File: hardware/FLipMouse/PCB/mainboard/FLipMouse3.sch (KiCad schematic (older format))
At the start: 85 parts, among them J1 SJ2-3574A, J2 SJ2-3574A, J3 M50-3900542, J4 Conn_ARM_JTAG_SWD_10, J5 Conn_02x05_Odd_Even, J6 USB_OTG, J7 Conn_01x06, Q1 BC847, Q2 BC847, Q3 BSH108, Q4 BSH108, Q5 BSH108, SW1 SW_Push, SW2 SW_Push, U1 ESP32-WROOM, U2 TSOP4838, U3 LPC11U24FBD, U4 TSR_1-2433, U5 MPXV7007GP, Y1 JA-12.000-18-DFE

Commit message: changed schematic for prototyp B: -) Added VPP as 3v3, always on (supplied by a new LDO) -) Removed GNDD, one GND for this PCB -) Added p-channel FET for switching on/off the VBUS power -) Moved parts from VBUS (always on) to the switched VBUS_SW -) Added VCC_SW, which is 3v3, powered from the high-power GPIO (PIO0_7) of the LPC; powers the MPX + FSR + Mic
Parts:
- removed Q5: BSH108, Package_TO_SOT_SMD:SOT-23, symbol Device:Q_NMOS_GSD
- added C? (x2): 1u, Capacitor_SMD:C_0805_2012Metric, symbol Device:C
- added Q?: Si2301, Package_TO_SOT_SMD:SOT-23, symbol Device:Q_PMOS_GSD
- added R?: 10k, Resistor_SMD:R_0603_1608Metric, symbol Device:R
- added U?: AP2127N-3.3, Package_TO_SOT_SMD:SOT-23, symbol Regulator_Linear:AP2127N-3.3
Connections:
- net GNDD is gone; now on net GND: C10.2, C15.2, C17.2, C18.2, C3.1, C4.1, C7.2, D2.2 (GND), D3.1 (VSS), J1.1 (Pin_1), J2.1 (Pin_1), J3.2 (Pin_2), J5.1 (Pin_1), J7.1 (Pin_1), Q3.2 (S), Q4.2 (S), R12.1, R13.1, R14.1, R15.1, R16.2, SW1.2, SW2.2, U1.1 (GND), U1.15 (GND), U1.38 (GND), U1.39 (GND-PAD), U2.2 (GND), U5.3 (GND)
- net +3V3: now also J3.4 (Pin_4); no longer C11.1, C13.1, C16.1, C8.1, C9.1, J3.1 (Pin_1), J4.1 (VCC), R8.2, R9.2, U3.44 (VDD), U3.8 (VDD)
- net ESP_POWER: now also Q?.1 (G), R?.2
- net FSR1: no longer U1.8 (IO32)
- net FSR2: no longer U1.7 (IO35)
- net FSR3: no longer U1.4 (SENSOR_VP)
- net FSR4: no longer U1.5 (SENSOR_VN)
- net GND: now also C?.2, C?.2, U?.1 (GND); no longer J3.4 (Pin_4)
- net PRESSURE: no longer U1.6 (IO34)
- net VBUS: now also C?.1, Q?.2 (S), R?.1, U?.3 (VI); no longer C12.1, C14.1, D4.2 (A), D8.2 (A), U4.1 (Vin)
- net VCC_SW: now reaches U3.23 (PIO0_7/~CTS~)
- net VCC_SW: now also J3.1 (Pin_1)
- new net VBUS_SW: C12.1, C14.1, D4.2 (A), D8.2 (A), Q?.3 (D), U4.1 (Vin)
- new net VPP: C11.1, C13.1, C16.1, C8.1, C9.1, C?.1, J4.1 (VCC), R8.2, R9.2, U3.44 (VDD), U3.8 (VDD), U?.2 (VO)
- no-connect marks 35 -> 39
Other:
- note added: "3V3 LDO - always on"
- note added: "Note:\n+3V3 is supplied by TSR-1 \nand can be switched off.\nVPP is a low-power supply \nvoltage, always on.\nVBUS is the USB 5V\nVBUS_SW is USB 5V\nswitched on/off\nVCC_SW is powered\nby an LPC GPIO"
- note added: "Power switch for +5V VBUS"
- note added: "or: RT9161-33"
- note removed: "Necessary to meet \nUSB specs in sleep\nmode current\nconsumption"
- note removed: "PowerOff for ESP32"

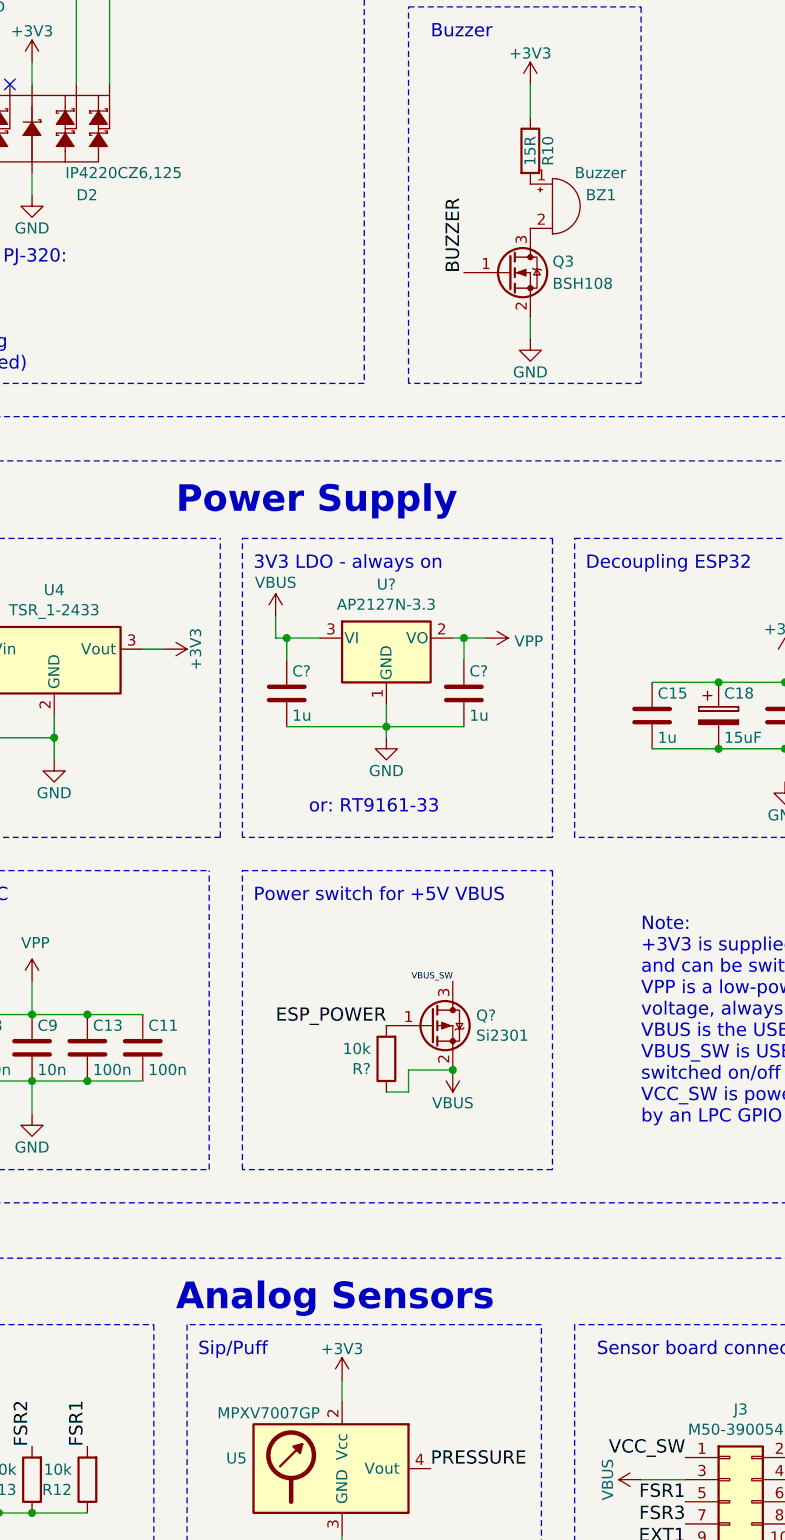
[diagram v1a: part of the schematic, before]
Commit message: Added free-wheeling diode for buzzer (according to datasheet) Moved MPX power to LPC pin
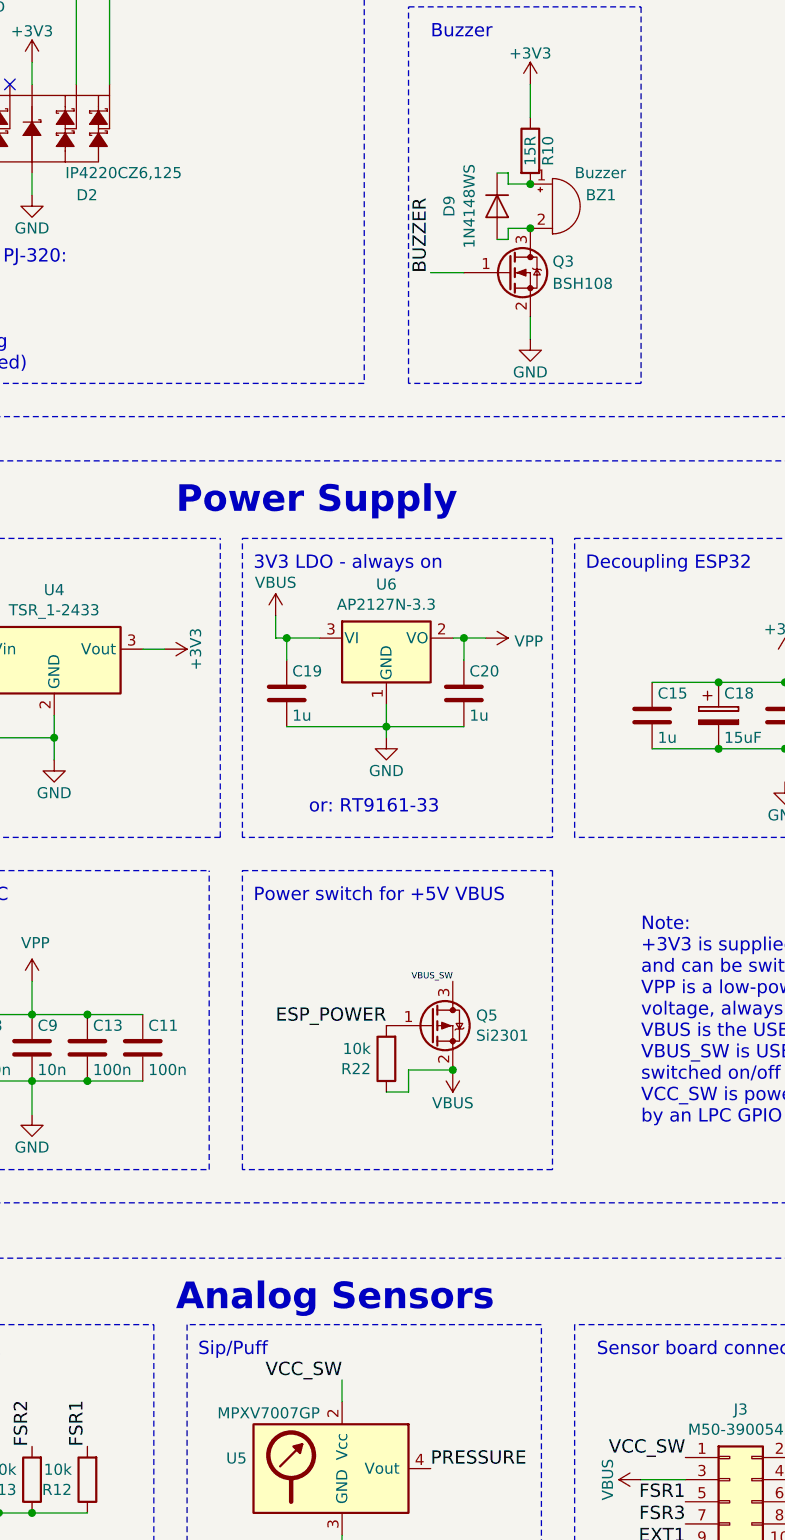
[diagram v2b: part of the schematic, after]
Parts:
- added D9: 1N4148WS, Diode_SMD:D_SOD-323, symbol Device:D
- gave numbers to parts that had none: 5
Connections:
- net +3V3: no longer U5.2 (Vcc)
- net VCC_SW: now also U5.2 (Vcc)
- net at BZ1.1 (-), R10.2: now also D9.1 (K)
- net at BZ1.2 (+), Q3.3 (D): now also D9.2 (A)
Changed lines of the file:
@@
 Text Label 6600 2800 2    60   ~ 0
 BUZZER
-Text Label 13650 3650 1    60   ~ 0
+Text Label 13500 3650 1    60   ~ 0
 BUZZER
 Text Label 15250 1300 0    60   ~ 0
@@
 Text Label 13500 9050 0    60   ~ 0
 PRESSURE
-$Comp
-L power:+3V3 #PWR0118
-U 1 1 5BCC3E24
-P 13100 8650
-F 0 "#PWR0118" H 13100 8500 50  0001 C CNN
-F 1 "+3V3" H 13100 8790 50  0000 C CNN
-F 2 "" H 13100 8650 50  0001 C CNN
-F 3 "" H 13100 8650 50  0001 C CNN
-	1    13100 8650
-	1    0    0    -1
-$EndComp
 Wire Wire Line
 	11700 3300 11700 3200
@@
 Feed-Through Routing - workaround
 $Comp
-L power:VPP #PWR?
+L power:VPP #PWR029
 U 1 1 5C872CD7
 P 13750 5300
-F 0 "#PWR?" H 13750 5150 50  0001 C CNN
+F 0 "#PWR029" H 13750 5150 50  0001 C CNN
 F 1 "VPP" V 13765 5428 50  0000 L CNN
 F 2 "" H 13750 5300 50  0001 C CNN
@@
 Note:\n+3V3 is supplied by TSR-1 \nand can be switched off.\nVPP is a low-power supply \nvoltage, always on.\nVBUS is the USB 5V\nVBUS_SW is USB 5V\nswitched on/off\nVCC_SW is powered\nby an LPC GPIO
 $Comp
-L power:GND #PWR?
+L power:GND #PWR033
 U 1 1 5C8739E0
 P 15100 5950
-F 0 "#PWR?" H 15100 5700 50  0001 C CNN
+F 0 "#PWR033" H 15100 5700 50  0001 C CNN
 F 1 "GND" H 15100 5800 50  0000 C CNN
 F 2 "" H 15100 5950 50  0001 C CNN
@@
 $EndComp
 $Comp
-L power:GND #PWR?
+L power:GND #PWR044
 U 1 1 5C8749EE
 P 13100 9500
-F 0 "#PWR?" H 13100 9250 50  0001 C CNN
+F 0 "#PWR044" H 13100 9250 50  0001 C CNN
 F 1 "GND" H 13100 9350 50  0000 C CNN
 F 2 "" H 13100 9500 50  0001 C CNN
@@
 $EndComp
 $Comp
-L power:GND #PWR?
+L power:GND #PWR043
 U 1 1 5C874AF8
 P 11550 9400
-F 0 "#PWR?" H 11550 9150 50  0001 C CNN
+F 0 "#PWR043" H 11550 9150 50  0001 C CNN
 F 1 "GND" H 11550 9250 50  0000 C CNN
 F 2 "" H 11550 9400 50  0001 C CNN
@@
 $EndComp
 $Comp
-L power:GND #PWR?
+L power:GND #PWR040
 U 1 1 5C874EB5
 P 7000 9000
-F 0 "#PWR?" H 7000 8750 50  0001 C CNN
+F 0 "#PWR040" H 7000 8750 50  0001 C CNN
 F 1 "GND" H 7000 8850 50  0000 C CNN
 F 2 "" H 7000 9000 50  0001 C CNN
@@
 $EndComp
 $Comp
-L power:GND #PWR?
+L power:GND #PWR037
 U 1 1 5C875619
 P 6700 7500
-F 0 "#PWR?" H 6700 7250 50  0001 C CNN
+F 0 "#PWR037" H 6700 7250 50  0001 C CNN
 F 1 "GND" H 6700 7350 50  0000 C CNN
 F 2 "" H 6700 7500 50  0001 C CNN
@@
 $EndComp
 $Comp
-L power:GND #PWR?
+L power:GND #PWR038
 U 1 1 5C875982
 P 9050 7600
-F 0 "#PWR?" H 9050 7350 50  0001 C CNN
+F 0 "#PWR038" H 9050 7350 50  0001 C CNN
 F 1 "GND" H 9050 7450 50  0000 C CNN
 F 2 "" H 9050 7600 50  0001 C CNN
@@
 $EndComp
 $Comp
-L power:GND #PWR?
+L power:GND #PWR024
 U 1 1 5C8830F6
 P 13950 3950
-F 0 "#PWR?" H 13950 3700 50  0001 C CNN
+F 0 "#PWR024" H 13950 3700 50  0001 C CNN
 F 1 "GND" H 13950 3800 50  0000 C CNN
 F 2 "" H 13950 3950 50  0001 C CNN
@@
 $EndComp
 $Comp
-L power:GND #PWR?
+L power:GND #PWR017
 U 1 1 5C883359
 P 11700 3300
-F 0 "#PWR?" H 11700 3050 50  0001 C CNN
+F 0 "#PWR017" H 11700 3050 50  0001 C CNN
 F 1 "GND" H 11700 3150 50  0000 C CNN
 F 2 "" H 11700 3300 50  0001 C CNN
@@
 $EndComp
 $Comp
-L power:GND #PWR?
+L power:GND #PWR015
 U 1 1 5C88365B
 P 11500 2300
-F 0 "#PWR?" H 11500 2050 50  0001 C CNN
+F 0 "#PWR015" H 11500 2050 50  0001 C CNN
 F 1 "GND" H 11500 2150 50  0000 C CNN
 F 2 "" H 11500 2300 50  0001 C CNN
@@
 $EndComp
 $Comp
-L power:GND #PWR?
+L power:GND #PWR014
 U 1 1 5C88370E
 P 12750 2150
-F 0 "#PWR?" H 12750 1900 50  0001 C CNN
+F 0 "#PWR014" H 12750 1900 50  0001 C CNN
 F 1 "GND" H 12750 2000 50  0000 C CNN
 F 2 "" H 12750 2150 50  0001 C CNN
@@
 $EndComp
 $Comp
-L power:GND #PWR?
+L power:GND #PWR013
 U 1 1 5C8837C1
 P 14000 2050
-F 0 "#PWR?" H 14000 1800 50  0001 C CNN
+F 0 "#PWR013" H 14000 1800 50  0001 C CNN
 F 1 "GND" H 14000 1900 50  0000 C CNN
 F 2 "" H 14000 2050 50  0001 C CNN
@@
 $EndComp
 $Comp
-L power:GND #PWR?
+L power:GND #PWR05
 U 1 1 5C883A1A
 P 14900 1800
-F 0 "#PWR?" H 14900 1550 50  0001 C CNN
+F 0 "#PWR05" H 14900 1550 50  0001 C CNN
 F 1 "GND" H 14900 1650 50  0000 C CNN
 F 2 "" H 14900 1800 50  0001 C CNN
@@
 $EndComp
 $Comp
-L power:GND #PWR?
+L power:GND #PWR011
 U 1 1 5C883ACD
 P 15250 1800
-F 0 "#PWR?" H 15250 1550 50  0001 C CNN
+F 0 "#PWR011" H 15250 1550 50  0001 C CNN
 F 1 "GND" H 15250 1650 50  0000 C CNN
 F 2 "" H 15250 1800 50  0001 C CNN
@@
 $EndComp
 $Comp
-L power:GND #PWR?
+L power:GND #PWR018
 U 1 1 5C883E74
 P 8550 3550
-F 0 "#PWR?" H 8550 3300 50  0001 C CNN
+F 0 "#PWR018" H 8550 3300 50  0001 C CNN
 F 1 "GND" H 8550 3400 50  0000 C CNN
 F 2 "" H 8550 3550 50  0001 C CNN
@@
 $EndComp
 $Comp
-L power:GND #PWR?
+L power:GND #PWR020
 U 1 1 5C8841C9
 P 7100 3850
-F 0 "#PWR?" H 7100 3600 50  0001 C CNN
+F 0 "#PWR020" H 7100 3600 50  0001 C CNN
 F 1 "GND" H 7100 3700 50  0000 C CNN
 F 2 "" H 7100 3850 50  0001 C CNN
@@
 $EndComp
 $Comp
-L power:GND #PWR?
+L power:GND #PWR016
 U 1 1 5C884584
 P 5800 2550
-F 0 "#PWR?" H 5800 2300 50  0001 C CNN
+F 0 "#PWR016" H 5800 2300 50  0001 C CNN
 F 1 "GND" H 5800 2400 50  0000 C CNN
 F 2 "" H 5800 2550 50  0001 C CNN
@@
 $EndComp
 $Comp
-L power:GND #PWR?
+L power:GND #PWR026
 U 1 1 5C88530D
 P 8800 4850
-F 0 "#PWR?" H 8800 4600 50  0001 C CNN
+F 0 "#PWR026" H 8800 4600 50  0001 C CNN
 F 1 "GND" H 8800 4700 50  0000 C CNN
 F 2 "" H 8800 4850 50  0001 C CNN
@@
 $EndComp
 $Comp
-L Regulator_Linear:AP2127N-3.3 U?
+L Regulator_Linear:AP2127N-3.3 U6
 U 1 1 5C8893E9
 P 13300 5300
-F 0 "U?" H 13300 5542 50  0000 C CNN
+F 0 "U6" H 13300 5542 50  0000 C CNN
 F 1 "AP2127N-3.3" H 13300 5451 50  0000 C CNN
 F 2 "Package_TO_SOT_SMD:SOT-23" H 13300 5525 50  0001 C CIN
@@
 or: RT9161-33
 $Comp
-L power:GND #PWR?
+L power:GND #PWR030
 U 1 1 5C88964E
 P 13300 5750
-F 0 "#PWR?" H 13300 5500 50  0001 C CNN
+F 0 "#PWR030" H 13300 5500 50  0001 C CNN
 F 1 "GND" H 13300 5600 50  0000 C CNN
 F 2 "" H 13300 5750 50  0001 C CNN
@@
 	13750 5300 13650 5300
 $Comp
-L power:VBUS #PWR?
+L power:VBUS #PWR027
 U 1 1 5C8B1D87
 P 12800 5200
-F 0 "#PWR?" H 12800 5050 50  0001 C CNN
+F 0 "#PWR027" H 12800 5050 50  0001 C CNN
 F 1 "VBUS" H 12800 5350 50  0000 C CNN
 F 2 "" H 12800 5200 50  0001 C CNN
@@
 	12800 5300 12850 5300
 $Comp
-L Device:C C?
+L Device:C C19
 U 1 1 5C8BF836
 P 12850 5550
-F 0 "C?" H 12875 5650 50  0000 L CNN
+F 0 "C19" H 12875 5650 50  0000 L CNN
 F 1 "1u" H 12875 5450 50  0000 L CNN
 F 2 "Capacitor_SMD:C_0805_2012Metric" H 12888 5400 50  0001 C CNN
@@
 VCC_SW
 $Comp
-L power:+3V3 #PWR?
+L power:+3V3 #PWR042
 U 1 1 5C908208
 P 15300 9100
-F 0 "#PWR?" H 15300 8950 50  0001 C CNN
+F 0 "#PWR042" H 15300 8950 50  0001 C CNN
 F 1 "+3V3" H 15300 9240 50  0000 C CNN
 F 2 "" H 15300 9100 50  0001 C CNN
@@
 VBUS_SW
 $Comp
-L Device:Q_PMOS_GSD Q?
+L Device:Q_PMOS_GSD Q5
 U 1 1 5C918901
 P 13500 7050
-F 0 "Q?" H 13705 7096 50  0000 L CNN
+F 0 "Q5" H 13705 7096 50  0000 L CNN
 F 1 "Si2301" H 13705 7005 50  0000 L CNN
 F 2 "Package_TO_SOT_SMD:SOT-23" H 13700 7150 50  0001 C CNN
@@
 ESP_POWER
 $Comp
-L power:VBUS #PWR?
+L power:VBUS #PWR036
 U 1 1 5C928332
 P 13600 7250
-F 0 "#PWR?" H 13600 7100 50  0001 C CNN
+F 0 "#PWR036" H 13600 7100 50  0001 C CNN
 F 1 "VBUS" H 13600 7400 50  0000 C CNN
 F 2 "" H 13600 7250 50  0001 C CNN
@@
 VBUS_SW
 $Comp
-L power:VPP #PWR?
+L power:VPP #PWR02
 U 1 1 5C95589A
 P 4200 1300
-F 0 "#PWR?" H 4200 1150 50  0001 C CNN
+F 0 "#PWR02" H 4200 1150 50  0001 C CNN
 F 1 "VPP" V 4215 1428 50  0000 L CNN
 F 2 "" H 4200 1300 50  0001 C CNN
@@
 $EndComp
 $Comp
-L power:VPP #PWR?
+L power:VPP #PWR039
 U 1 1 5C955955
 P 2350 8500
-F 0 "#PWR?" H 2350 8350 50  0001 C CNN
+F 0 "#PWR039" H 2350 8350 50  0001 C CNN
 F 1 "VPP" H 2365 8673 50  0000 C CNN
 F 2 "" H 2350 8500 50  0001 C CNN
@@
 NoConn ~ 6600 2600
 $Comp
-L power:VPP #PWR?
+L power:VPP #PWR04
 U 1 1 5C9A0053
 P 1100 1600
-F 0 "#PWR?" H 1100 1450 50  0001 C CNN
+F 0 "#PWR04" H 1100 1450 50  0001 C CNN
 F 1 "VPP" H 1115 1773 50  0000 C CNN
 F 2 "" H 1100 1600 50  0001 C CNN
@@
 $EndComp
 $Comp
-L power:VPP #PWR?
+L power:VPP #PWR034
 U 1 1 5C9A06A3
 P 2850 6600
-F 0 "#PWR?" H 2850 6450 50  0001 C CNN
+F 0 "#PWR034" H 2850 6450 50  0001 C CNN
 F 1 "VPP" H 2865 6773 50  0000 C CNN
 F 2 "" H 2850 6600 50  0001 C CNN
@@
 SCL
 $Comp
-L Device:R R?
+L Device:R R22
 U 1 1 5C9A3CBF
 P 13300 7200
-F 0 "R?" H 13370 7246 50  0000 L CNN
+F 0 "R22" H 13370 7246 50  0000 L CNN
 F 1 "10k" H 13370 7155 50  0000 L CNN
 F 2 "Resistor_SMD:R_0603_1608Metric" V 13230 7200 50  0001 C CNN
@@
 Connection ~ 13600 7250
 $Comp
-L power:VPP #PWR?
+L power:VPP #PWR035
 U 1 1 5C9C2415
 P 11700 6850
-F 0 "#PWR?" H 11700 6700 50  0001 C CNN
+F 0 "#PWR035" H 11700 6700 50  0001 C CNN
 F 1 "VPP" H 11715 7023 50  0000 C CNN
 F 2 "" H 11700 6850 50  0001 C CNN
@@
 $EndComp
 $Comp
-L Device:C C?
+L Device:C C20
 U 1 1 5C8BF936
 P 13650 5550
-F 0 "C?" H 13675 5650 50  0000 L CNN
+F 0 "C20" H 13675 5650 50  0000 L CNN
 F 1 "1u" H 13675 5450 50  0000 L CNN
 F 2 "Capacitor_SMD:C_0805_2012Metric" H 13688 5400 50  0001 C CNN
@@
 	1    0    0    -1
 $EndComp
+Text Label 13100 8650 2    60   ~ 0
+VCC_SW
+$Comp
+L Device:D D9
+U 1 1 5C9C588F
+P 13800 3350
+F 0 "D9" H 13800 3134 50  0000 C CNN
+F 1 "1N4148WS" H 13800 3225 50  0000 C CNN
+F 2 "Diode_SMD:D_SOD-323" H 13800 3350 50  0001 C CNN
+F 3 "~" H 13800 3350 50  0001 C CNN
+	1    13800 3350
+	0    1    1    0
+$EndComp
+Wire Wire Line
+	13500 3650 13650 3650
+Wire Wire Line
+	13800 3200 13850 3200
+Wire Wire Line
+	13850 3200 13850 3250
+Wire Wire Line
+	13850 3250 13950 3250
+Connection ~ 13950 3250
+Wire Wire Line
+	13800 3500 13850 3500
+Wire Wire Line
+	13850 3500 13850 3450
+Wire Wire Line
+	13850 3450 13950 3450
+Connection ~ 13950 3450
 $EndSCHEMATC
